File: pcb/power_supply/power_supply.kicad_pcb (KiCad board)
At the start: 2 copper layers, 60 x 99.5 mm, 25 parts, among them J1 LINE, J2 PWR_CH1, J3 PWR_CH2, J4 PWR_UI_BOARD, J5 EARTH, SW1 SW_DPDT_x2, U1 AP63203WU

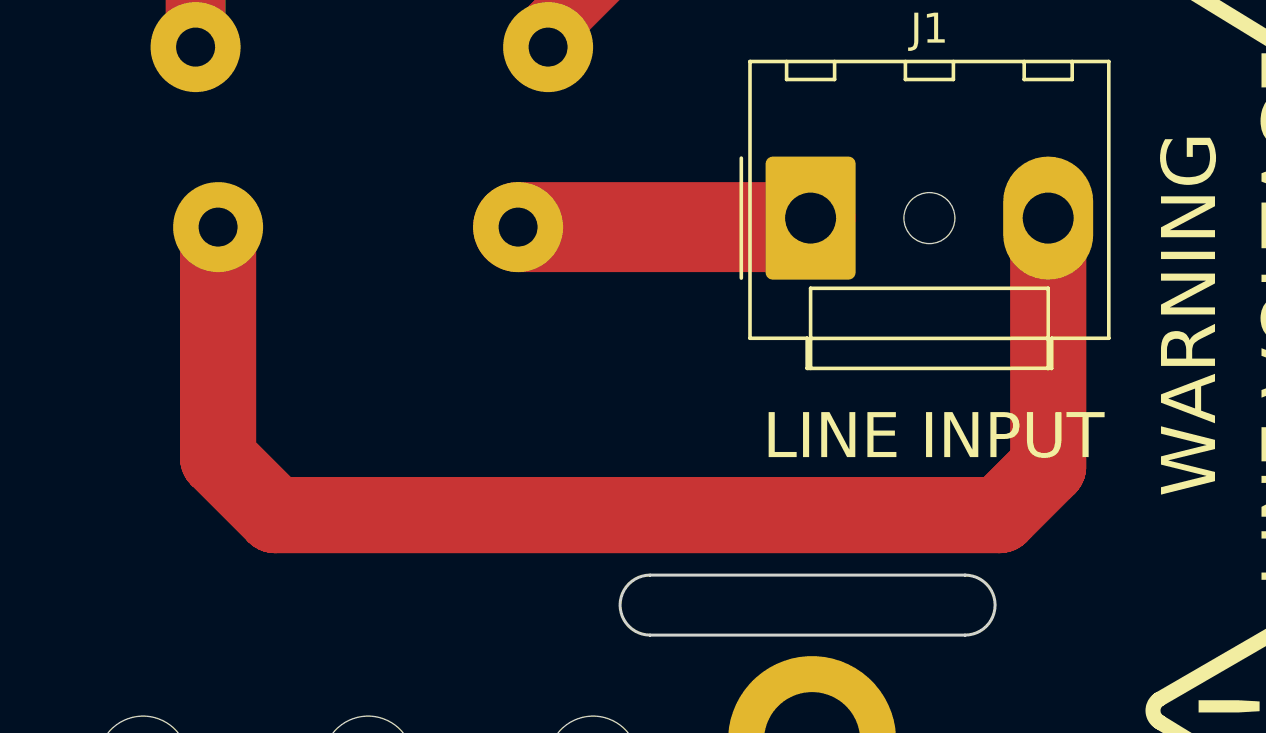
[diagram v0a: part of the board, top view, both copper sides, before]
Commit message: Update power supply  KiCAD project to v8 and fix incorrect R1 resistor value
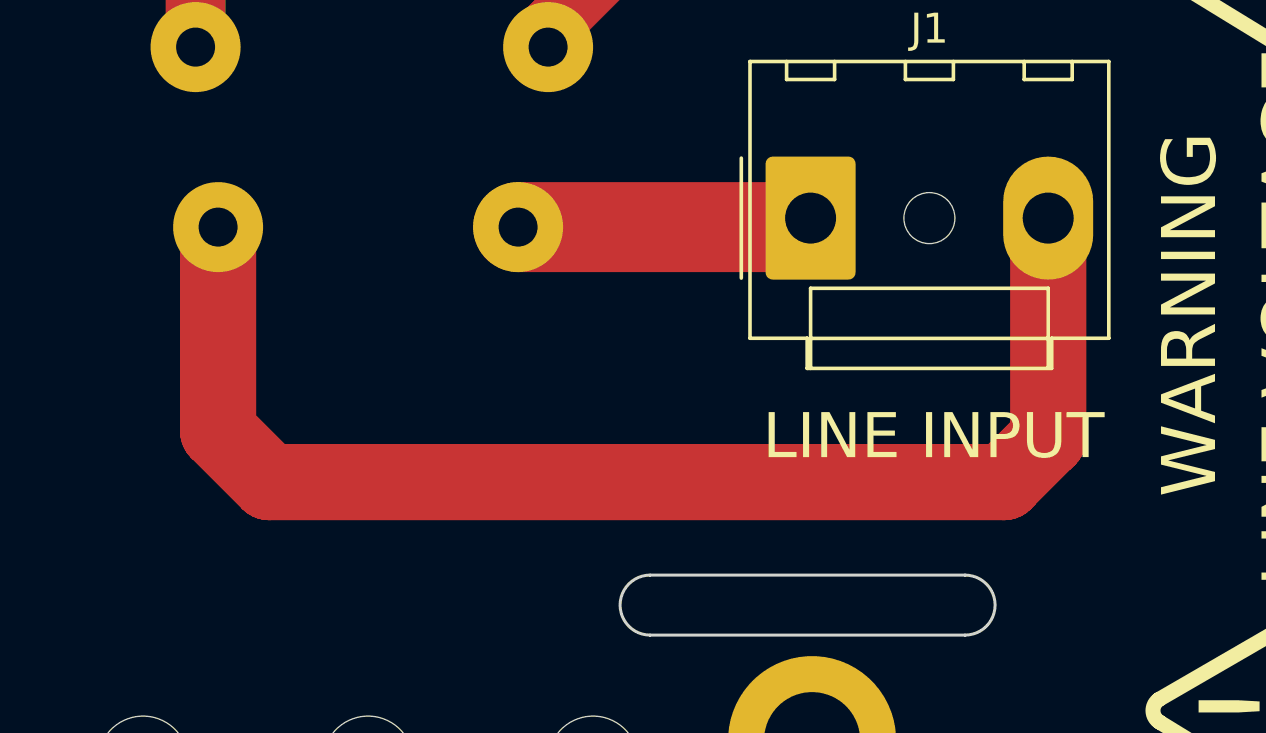
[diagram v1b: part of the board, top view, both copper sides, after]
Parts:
- R1: value 33 -> 15
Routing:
- net Net-(J1-Pin_3): track 45.1 -> 43.1 mm

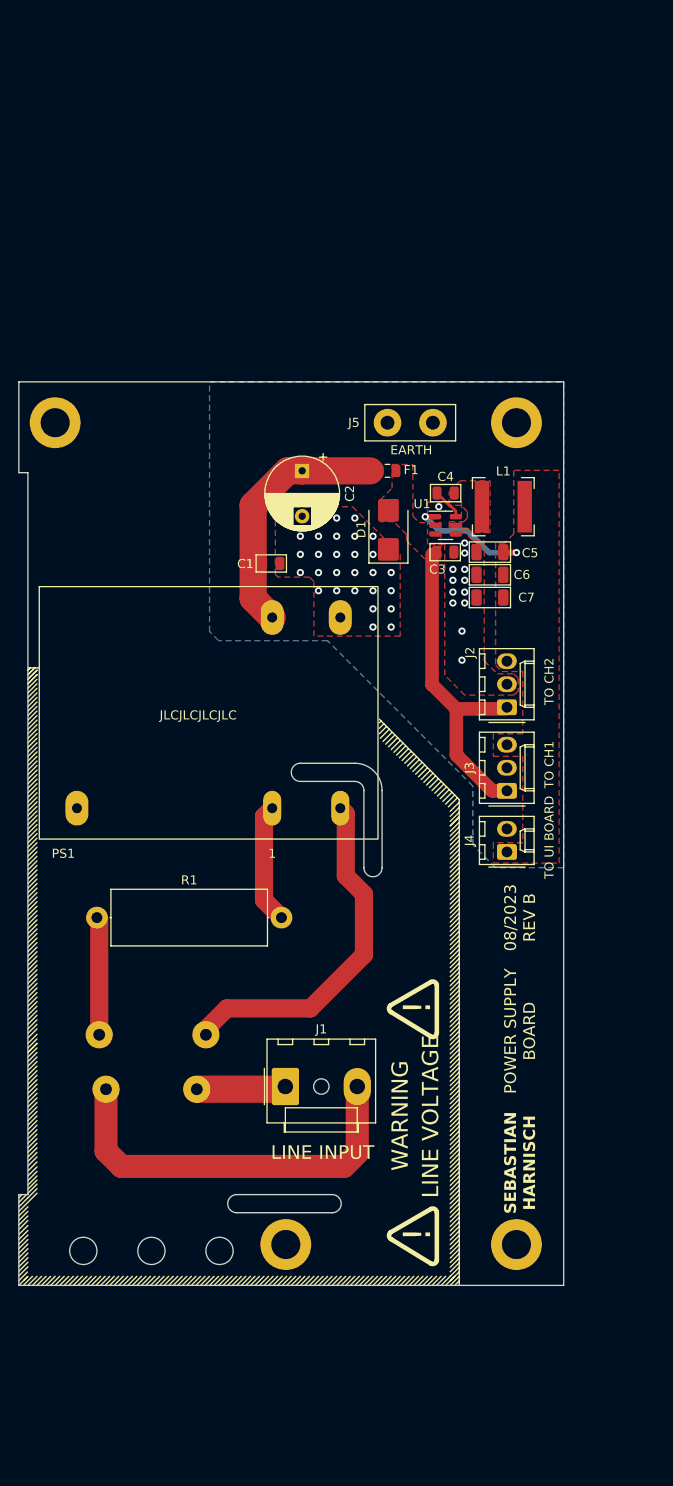
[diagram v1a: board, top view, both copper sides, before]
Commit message: Update to Kicad v9, new power supply board and other modifications
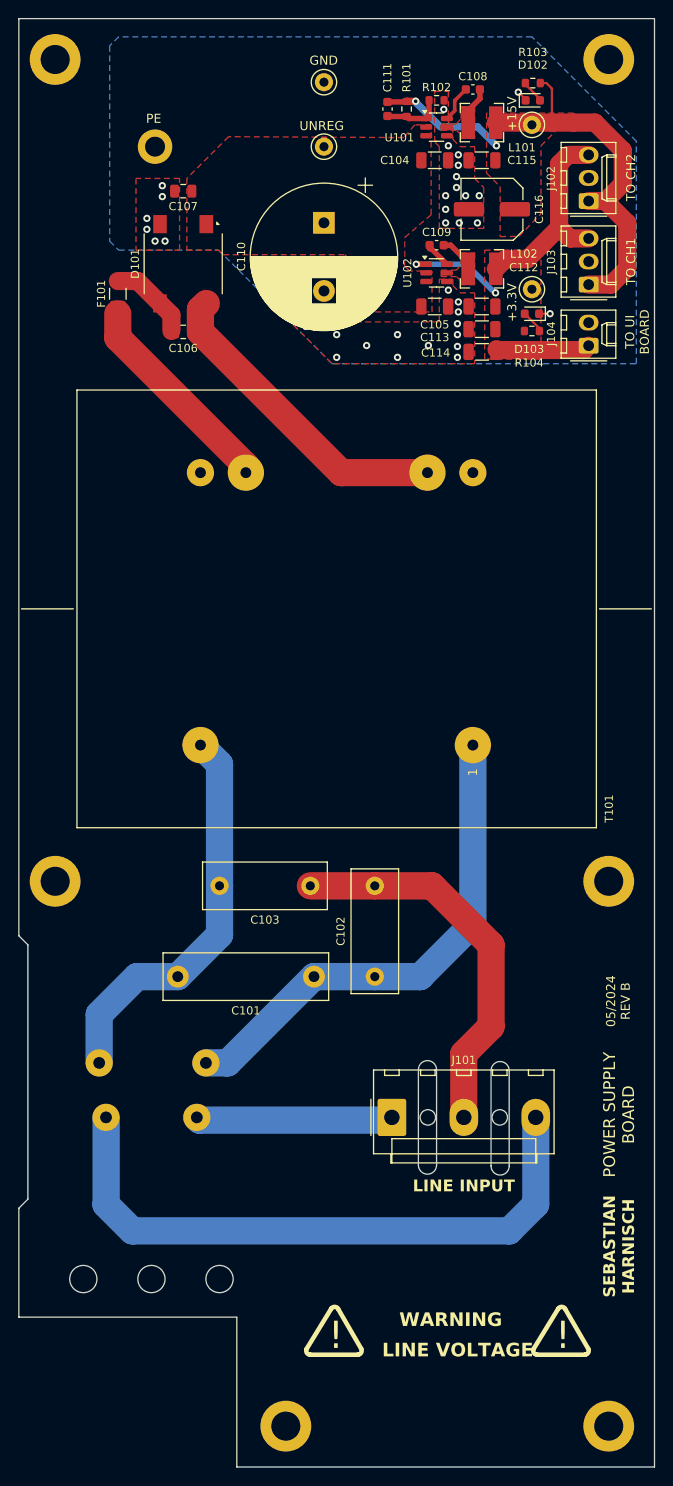
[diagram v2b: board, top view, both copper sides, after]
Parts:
- removed D1: SMBJ18CA, Diode_SMD:D_SMB
- removed J5: EARTH, 01_Sebastian:BananaJack_Connector
- removed PS1: TRACO_TMPW_10, 01_Sebastian:TRACO_TMPW_10
- removed R1: 15, Resistor_THT:R_Axial_DIN0617_L17.0mm_D6.0mm_P20.32mm_Horizontal
- added C101: 100n, Capacitor_THT:C_Rect_L18.0mm_W5.0mm_P15.00mm_FKS3_FKP3, F.Cu at (62.5, 131.0)
- added C102: 1n, Capacitor_THT:C_Rect_L13.5mm_W5.0mm_P10.00mm_FKS3_FKP3_MKS4, F.Cu at (69.2, 131.0)
- added C103: 1n, Capacitor_THT:C_Rect_L13.5mm_W5.0mm_P10.00mm_FKS3_FKP3_MKS4, F.Cu at (62.1, 121.0)
- added C104: 1u, Capacitor_SMD:C_1206_3216Metric, F.Cu at (75.8, 41.1)
- added C106: 100n, Capacitor_SMD:C_0805_2012Metric, F.Cu at (48.1, 60.0)
- added C108: 100n, Capacitor_SMD:C_0603_1608Metric, F.Cu at (80.0, 33.3)
- added C111: 56p, Capacitor_SMD:C_0603_1608Metric, F.Cu at (70.6, 35.5)
- added C115: 22u, Capacitor_SMD:C_1206_3216Metric, F.Cu at (81.0, 41.1)
- added C116: 68u, Capacitor_SMD:C_Elec_6.3x5.8, F.Cu at (82.1, 46.5)
- added D101: B250S2A-SLIM, Diode_SMD:Diode_Bridge_Diotec_SO-DIL-Slim, F.Cu at (48.1, 52.5)
- added D102: GR, LED_SMD:LED_0603_1608Metric, F.Cu at (86.6, 34.5)
- added D103: GR, LED_SMD:LED_0603_1608Metric, F.Cu at (86.5, 58.0)
- added H105: M3, MountingHole:MountingHole_3.2mm_M3_DIN965_Pad, F.Cu at (34.0, 30.0)
- added H106: M3, MountingHole:MountingHole_3.2mm_M3_DIN965_Pad, F.Cu at (95.0, 30.0)
- added H107: M3, MountingHole:MountingHole_2.2mm_M2_DIN965_Pad, F.Cu at (45.0, 39.6)
- added L101: 10u, Inductor_SMD:L_Bourns-SRN4018, F.Cu at (81.0, 37.0)
- added LOGO101: SYMBOL_TRIANGLE_WARNING, 01_Sebastian:Triangle_Warning, B.Cu at (89.8, 170.7)
- added LOGO101: SYMBOL_TRIANGLE_WARNING, 01_Sebastian:Triangle_Warning, B.Cu at (64.8, 170.7)
- added R101: 270k, Resistor_SMD:R_0603_1608Metric, F.Cu at (72.7, 35.5)
- added R102: 15k, Resistor_SMD:R_0603_1608Metric, F.Cu at (76.0, 34.5)
- added R103: 62k, Resistor_SMD:R_0603_1608Metric, F.Cu at (86.6, 32.6)
- added R104: 6.2k, Resistor_SMD:R_0603_1608Metric, F.Cu at (86.5, 59.9)
- added T101: Transformer_1P_1S, 01_Sebastian:BLOCK_VC16_1, F.Cu at (80.0, 105.5)
- added TP101: +15V, TestPoint:TestPoint_Keystone_5000-5004_Miniature, F.Cu at (86.5, 37.2)
- added TP102: +3.3V, TestPoint:TestPoint_Keystone_5000-5004_Miniature, F.Cu at (86.5, 55.3)
- added TP103: UNREG, TestPoint:TestPoint_Keystone_5000-5004_Miniature, F.Cu at (63.6, 39.6)
- added TP104: GND, TestPoint:TestPoint_Keystone_5000-5004_Miniature, F.Cu at (63.6, 32.5)
- added U101: AP63200WU, Package_TO_SOT_SMD:TSOT-23-6, F.Cu at (76.0, 37.5)
- C105: renamed from C3; footprint 01_Sebastian:C_0805_2012Metric_Box -> Capacitor_SMD:C_1206_3216Metric
- C107: renamed from C1; footprint 01_Sebastian:C_0805_2012Metric_Box -> Capacitor_SMD:C_0805_2012Metric
- C109: renamed from C4; footprint 01_Sebastian:C_0805_2012Metric_Box -> Capacitor_SMD:C_0603_1608Metric
- C110: renamed from C2; value 220u -> 1000u; footprint Capacitor_THT:CP_Radial_D8.0mm_P5.00mm -> Capacitor_THT:CP_Radial_D16.0mm_P7.50mm
- C112: renamed from C5; footprint 01_Sebastian:C_1206_3216Metric_Box -> Capacitor_SMD:C_1206_3216Metric
- C113: renamed from C6; footprint 01_Sebastian:C_1206_3216Metric_Box -> Capacitor_SMD:C_1206_3216Metric
- C114: renamed from C7; footprint 01_Sebastian:C_1206_3216Metric_Box -> Capacitor_SMD:C_1206_3216Metric
- F101: renamed from F1; footprint Fuse:Fuse_0805_2012Metric -> Fuse:Fuse_1206_3216Metric
- J101: renamed from J1; footprint Connector_Molex:Molex_KK-396_A-41791-0003_1x03_P3.96mm_Vertical -> Connector_Molex:Molex_KK-396_A-41791-0005_1x05_P3.96mm_Vertical
- L102: renamed from L1; footprint Inductor_SMD:L_Bourns-SRN6028 -> Inductor_SMD:L_Bourns-SRN4018
- moved J103 56.5 mm to (92.8, 54.8)
- moved J102 56.5 mm to (92.8, 45.6)
- moved J104 56.5 mm to (92.8, 61.5)
- moved H103 51.5 mm to (95.0, 120.5)
- moved H104 50.5 mm to (34.0, 120.5)
- moved C107 42.1 mm to (48.1, 44.5), turned to 180 degrees
- moved LOGO102 39.4 mm to (89.8, 170.7), turned to 0 degrees
- moved F101 35.5 mm to (40.9, 55.8), turned to 90 degrees
- moved U102 27.8 mm to (76.0, 53.5)
- moved C110 27.4 mm to (63.6, 48.0)
- moved C109 27.3 mm to (76.0, 50.5)
- moved C105 27.1 mm to (75.8, 57.2)
- moved C112 27.1 mm to (81.0, 57.2)
- moved C113 27.1 mm to (81.0, 59.7)
- moved C114 27.1 mm to (81.0, 62.2)
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- renumbered H1 to H101, H2 to H102, H3 to H103, H4 to H104, J2 to J102, J3 to J103, J4 to J104, LOGO1 to LOGO101, LOGO2 to LOGO102, SW1 to SW101, U1 to U102
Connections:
- C105 pad 1: +15V -> +18V
- C105 pad 2: GND -> Earth
- C107 pad 1: Net-(PS1-+V_{out}) -> +18V
- C107 pad 2: GND -> Earth
- C110 pad 1: Net-(PS1-+V_{out}) -> +18V
- C110 pad 2: GND -> Earth
- C112 pad 2: GND -> Earth
- C113 pad 2: GND -> Earth
- C114 pad 2: GND -> Earth
- F101 pad 1: Net-(PS1-+V_{out}) -> Net-(T101-SB)
- F101 pad 2: +15V -> Net-(C106-Pad1)
- J101 pad 3: Net-(J1-Pin_3) -> Earth
- J102 pad 2: GND -> Earth
- J103 pad 2: GND -> Earth
- J104 pad 2: GND -> Earth
- SW101 pad 5: Net-(J1-Pin_3) -> Net-(J101-Pin_5)
- U102 pad 2: +15V -> +18V
- U102 pad 3: +15V -> +18V
- U102 pad 4: GND -> Earth
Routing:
- net Net-(J101-Pin_5): track 0.00 -> 68.9 mm
- net Earth: track 0.00 -> 45.3 mm, vias 0 -> 46
- net Net-(J1-Pin_3): track 43.1 -> 0.00 mm
- net Net-(T101-SA): track 0.00 -> 34.8 mm
- net Net-(SW101B-C): track 13.0 -> 44.0 mm
- net +3.3V: track 14.3 -> 44.9 mm
- net Net-(PS1-+V_{out}): track 27.7 -> 0.00 mm
- net Net-(T101-SB): track 0.00 -> 23.3 mm
- net +15V: track 36.0 -> 57.4 mm, vias 0 -> 2
- net Net-(SW101A-C): track 38.6 -> 55.4 mm
- net Net-(PS1-N): track 13.2 -> 0.00 mm
- net Net-(J101-Pin_1): track 9.87 -> 21.7 mm
- net Net-(C106-Pad1): track 0.00 -> 9.22 mm
- net Net-(U101-FB): track 0.00 -> 6.51 mm
- net Net-(U101-SW): track 0.00 -> 4.19 mm
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- added copper zone on F.Cu, net +18V
- added copper zone on B.Cu, net Earth
- added copper zone on F.Cu, net Earth
- added copper zone on F.Cu, net Net-(U101-SW)
- removed copper zone on B.Cu, net GND
- removed copper zone on F.Cu, net GND
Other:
- board size 60 x 99.5 mm -> 70 x 159.5 mm
- board text added: "+15V"
- board text added: "+3.3V"
- board text added: "05/2024 REV B"
- board text added: "GND"
- board text added: "PE"
- board text added: "UNREG"
- board text removed: "08/2023 REV B"
- board text removed: "EARTH"
- board text removed: "JLCJLCJLCJLC"
